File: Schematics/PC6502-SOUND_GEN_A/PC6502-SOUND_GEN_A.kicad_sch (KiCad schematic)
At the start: 32 parts, among them J1 BUS, J2 NCO_OUT, J3 SND0/SND1, J5 Conn_02x05_Odd_Even, U10 74HC00, U2 74HC245, U4 ATF1504AS, U5 74AHCT244, U6 74AHCT244, U7 74HC14, U9 74HC74, X1 CXO_DIP8

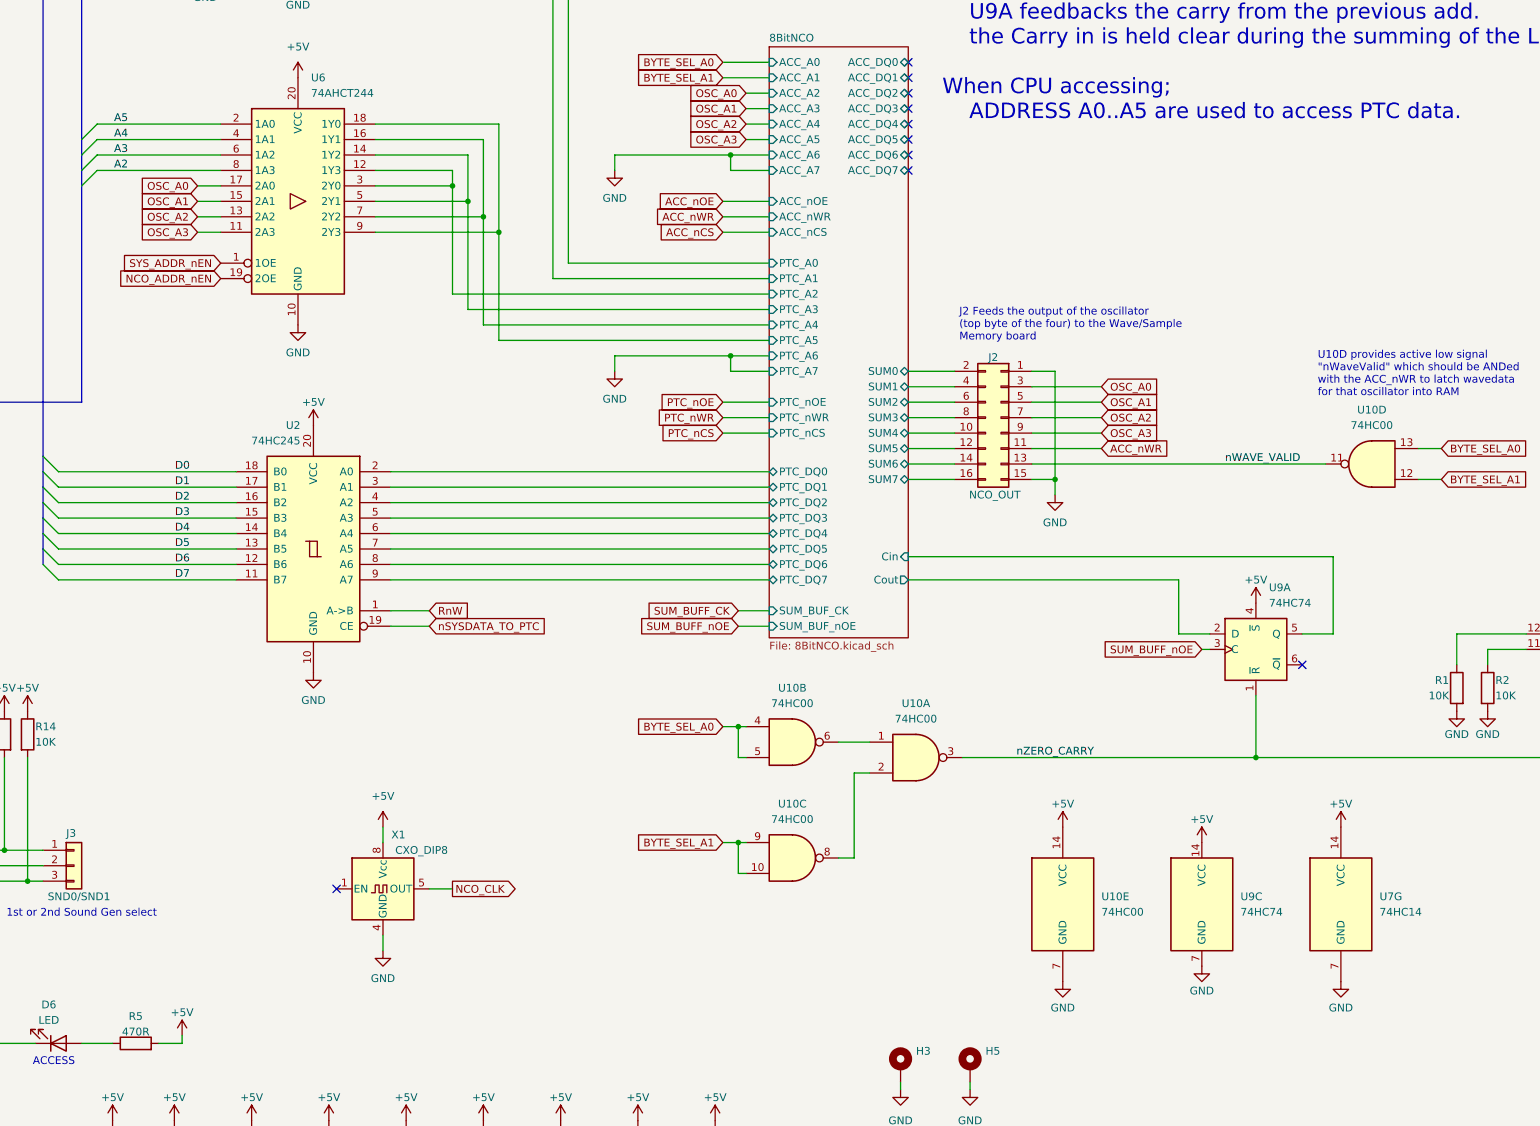
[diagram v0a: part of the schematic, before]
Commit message: Created V1.1 Schematic and PCB
A LOT of changes from v1.00;
removed clock stretcher (will now live in the CPLD)
moved the USB interface direct to the PCB
changed power pins
Added extra capacitance
Used Grant Searle's OSI basic and memory map to bring up the board
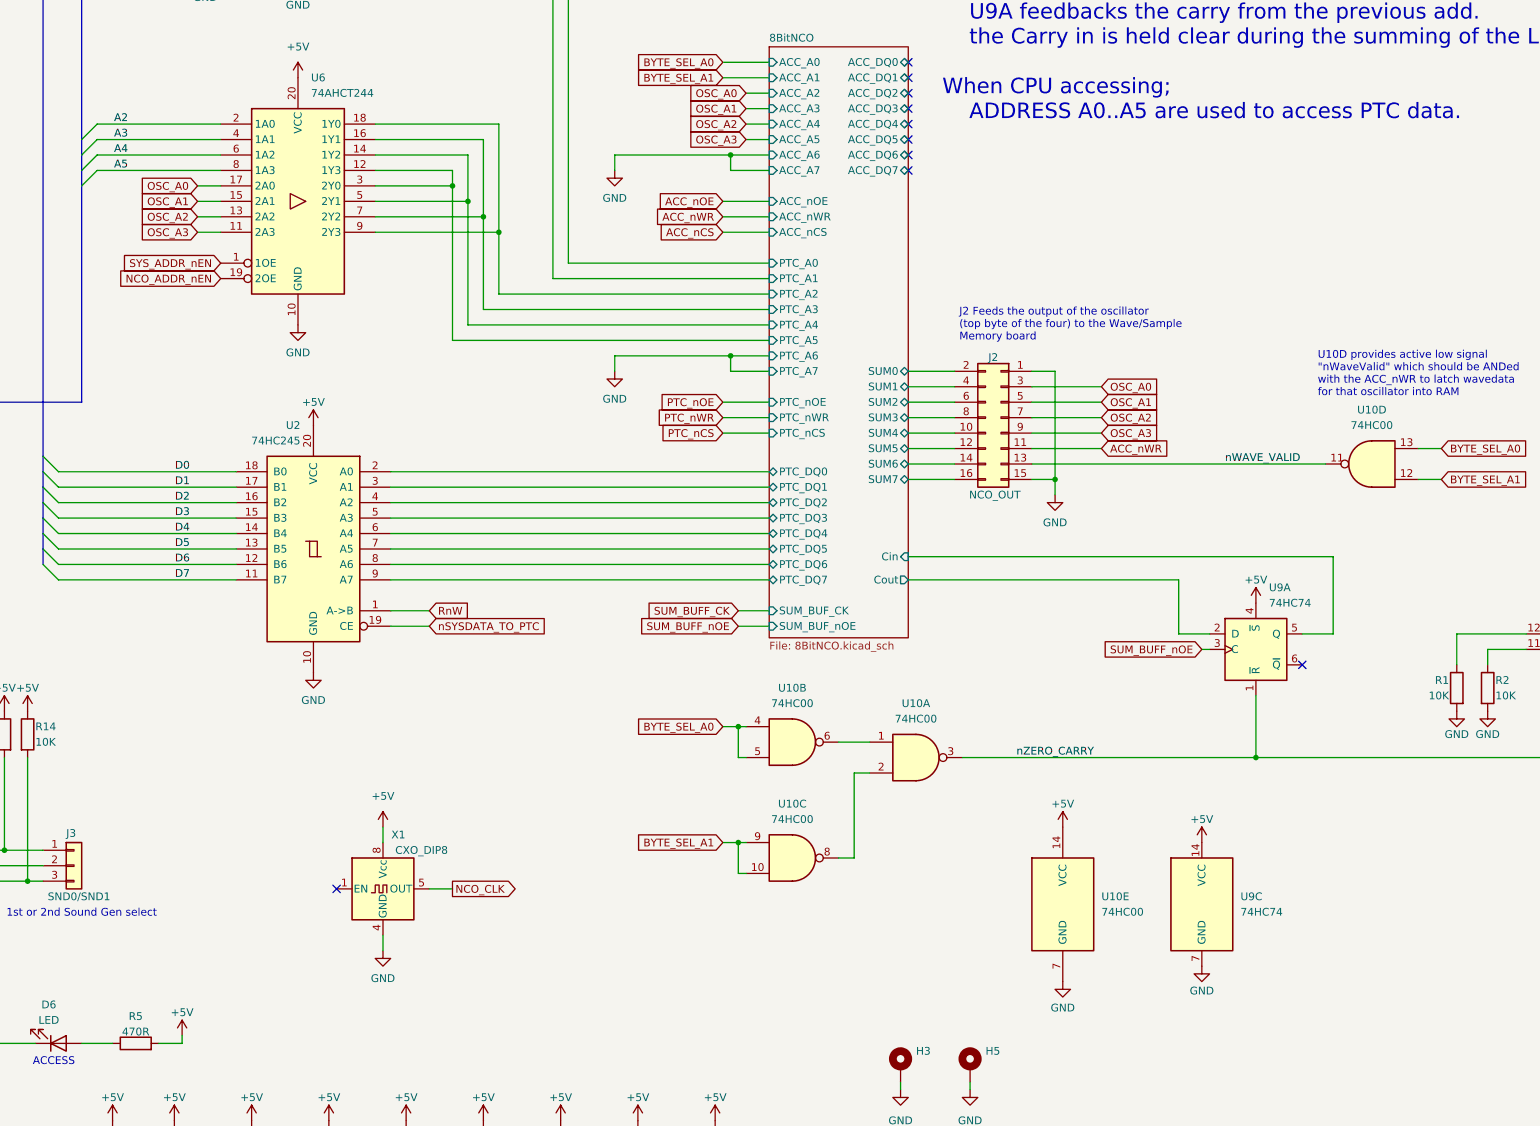
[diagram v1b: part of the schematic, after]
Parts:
- removed U7: 74HC14, Package_DIP:DIP-14_W7.62mm, symbol 74xx:74HC14
- U10, U9: footprint (none) -> Package_DIP:DIP-14_W7.62mm
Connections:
- net 8BitNCO/PTC_A2: now also U6.18 (1Y0), U6.9 (2Y3); no longer U6.12 (1Y3), U6.3 (2Y0)
- net 8BitNCO/PTC_A3: now also U6.16 (1Y1), U6.7 (2Y2); no longer U6.14 (1Y2), U6.5 (2Y1)
- net 8BitNCO/PTC_A4: now also U6.14 (1Y2), U6.5 (2Y1); no longer U6.16 (1Y1), U6.7 (2Y2)
- net 8BitNCO/PTC_A5: now also U6.12 (1Y3), U6.3 (2Y0); no longer U6.18 (1Y0), U6.9 (2Y3)
- net A2: now also U6.2 (1A0); no longer U6.8 (1A3)
- net A3: now also U6.4 (1A1); no longer U6.6 (1A2)
- net A4: now also U6.6 (1A2); no longer U6.4 (1A1)
- net A5: now also U6.8 (1A3); no longer U6.2 (1A0)

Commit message: Update KeyTFT CPLD
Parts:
- removed R14, R9: 10K, Resistor_SMD:R_0603_1608Metric_Pad0.98x0.95mm_HandSolder, symbol Device:R
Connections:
- net +5V: now also J1.12 (Pin_12), J1.16 (Pin_16), J1.20 (Pin_20), J1.24 (Pin_24), J1.28 (Pin_28), J1.32 (Pin_32), J1.36 (Pin_36), J1.4 (Pin_4), J1.40 (Pin_40), J1.44 (Pin_44), J1.48 (Pin_48), J1.8 (Pin_8), J3.1 (Pin_1); no longer J1.59 (Pin_59), J1.61 (Pin_61), J1.62 (Pin_62), J1.63 (Pin_63), J1.64 (Pin_64)
- net A6: now also U4.44 (I/OE1); no longer J3.2 (Pin_2)
- net ACC_nWR: now also U4.4 (I/O); no longer U4.11 (I/O/PD1)
- net CPU_CLK: no longer U4.43 (I/GCLK1)
- net GND: now also J1.64 (Pin_64), J3.3 (Pin_3); no longer J1.12 (Pin_12), J1.16 (Pin_16), J1.20 (Pin_20), J1.24 (Pin_24), J1.28 (Pin_28), J1.32 (Pin_32), J1.36 (Pin_36), J1.4 (Pin_4), J1.40 (Pin_40), J1.44 (Pin_44), J1.48 (Pin_48), J1.8 (Pin_8)
- net RnW: now also U4.43 (I/GCLK1); no longer U4.4 (I/O)
- net nBUSRQ: now also J1.61 (Pin_61); no longer J1.55 (Pin_55)
- net nRES: now also J1.63 (Pin_63); no longer J1.57 (Pin_57)
- net at U4.1 (I/GCLR): now also J3.2 (Pin_2); no longer J3.1 (Pin_1)
- net CLK renamed SYSCLK
- net nSLOW renamed nSLOW0
- new net RDY: J1.57 (Pin_57)
- new net nSLOW1: J1.55 (Pin_55)
- new net nVP: J1.59 (Pin_59)
- no-connect marks 20 -> 22
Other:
- note added: "CPU_CLK is the stretched version of CLK. Use nSLOW0 and nSLOW1 to slow the clock down"
- note removed: "I now realise that some peripherals need the stretched CPU clock, DOH! So I'll mod wire the CPU_CLOCK on the main CPU board to SP_CLK :("
- moved on the sheet: J3
